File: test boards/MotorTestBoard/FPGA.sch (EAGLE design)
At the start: 2 parts, among them X1 87758-4016, X2 87758-4016

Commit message: FPGA Labelling
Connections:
- new net M11A: X1-3.S
- new net M11B: X1-5.S
- new net M12A: X1-7.S
- new net M12B: X1-9.S
- new net M13A: X1-11.S
- new net M13B: X1-13.S
- new net M1EA: X1-4.S
- new net M1EB: X1-6.S
- new net M1H1: X1-8.S
- new net M1H2: X1-10.S
- new net M1H3: X1-12.S
- new net M21A: X1-27.S
- new net M21B: X1-29.S
- new net M22A: X1-31.S
- new net M22B: X1-33.S
- new net M23A: X1-35.S
- new net M23B: X1-37.S
- new net M2EA: X1-30.S
- new net M2EB: X1-32.S
- new net M2H1: X1-34.S
- new net M2H2: X1-36.S
- new net M2H3: X1-38.S
- new net M31A: X2-4.S
- new net M31B: X2-6.S
- new net M32A: X2-8.S
- new net M32B: X2-10.S
- new net M33A: X2-12.S
- new net M33B: X2-14.S
- new net M3EA: X2-3.S
- new net M3EB: X2-5.S
- new net M3H1: X2-7.S
- new net M3H2: X2-9.S
- new net M3H3: X2-11.S
- new net M41A: X2-28.S
- new net M41B: X2-30.S
- new net M42A: X2-32.S
- new net M42B: X2-34.S
- new net M43A: X2-36.S
- new net M43B: X2-38.S
- new net M4EA: X2-29.S
- new net M4EB: X2-31.S
- new net M4H1: X2-33.S
- new net M4H2: X2-35.S
- new net M4H3: X2-37.S
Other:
- moved on the sheet: X1-1, X1-10, X1-11, X1-12, X1-13, X1-14, X1-15, X1-16, X1-17, X1-18, X1-19, X1-2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

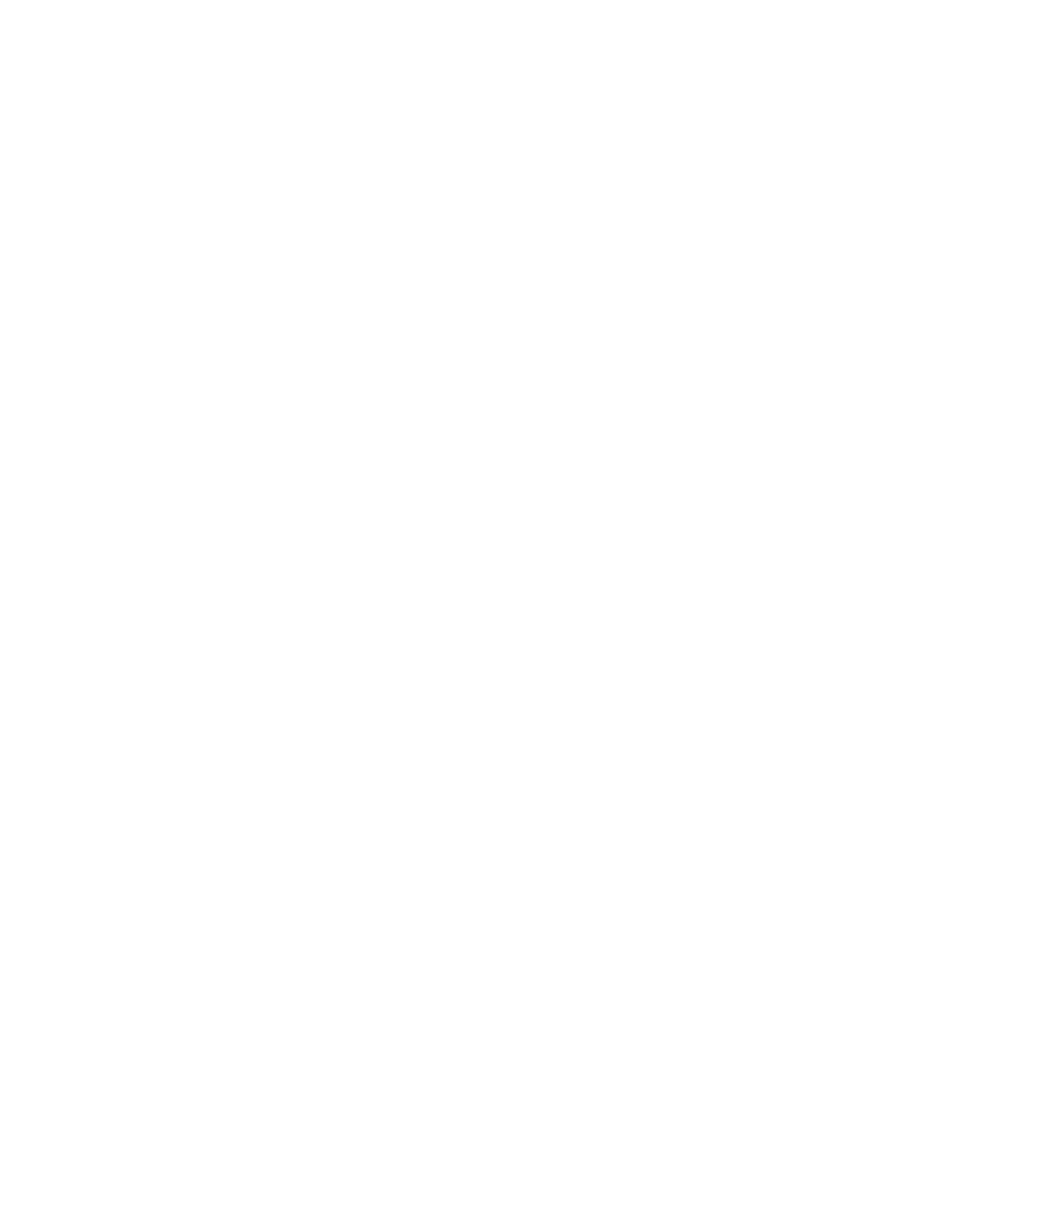
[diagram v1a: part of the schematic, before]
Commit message: motor driver add
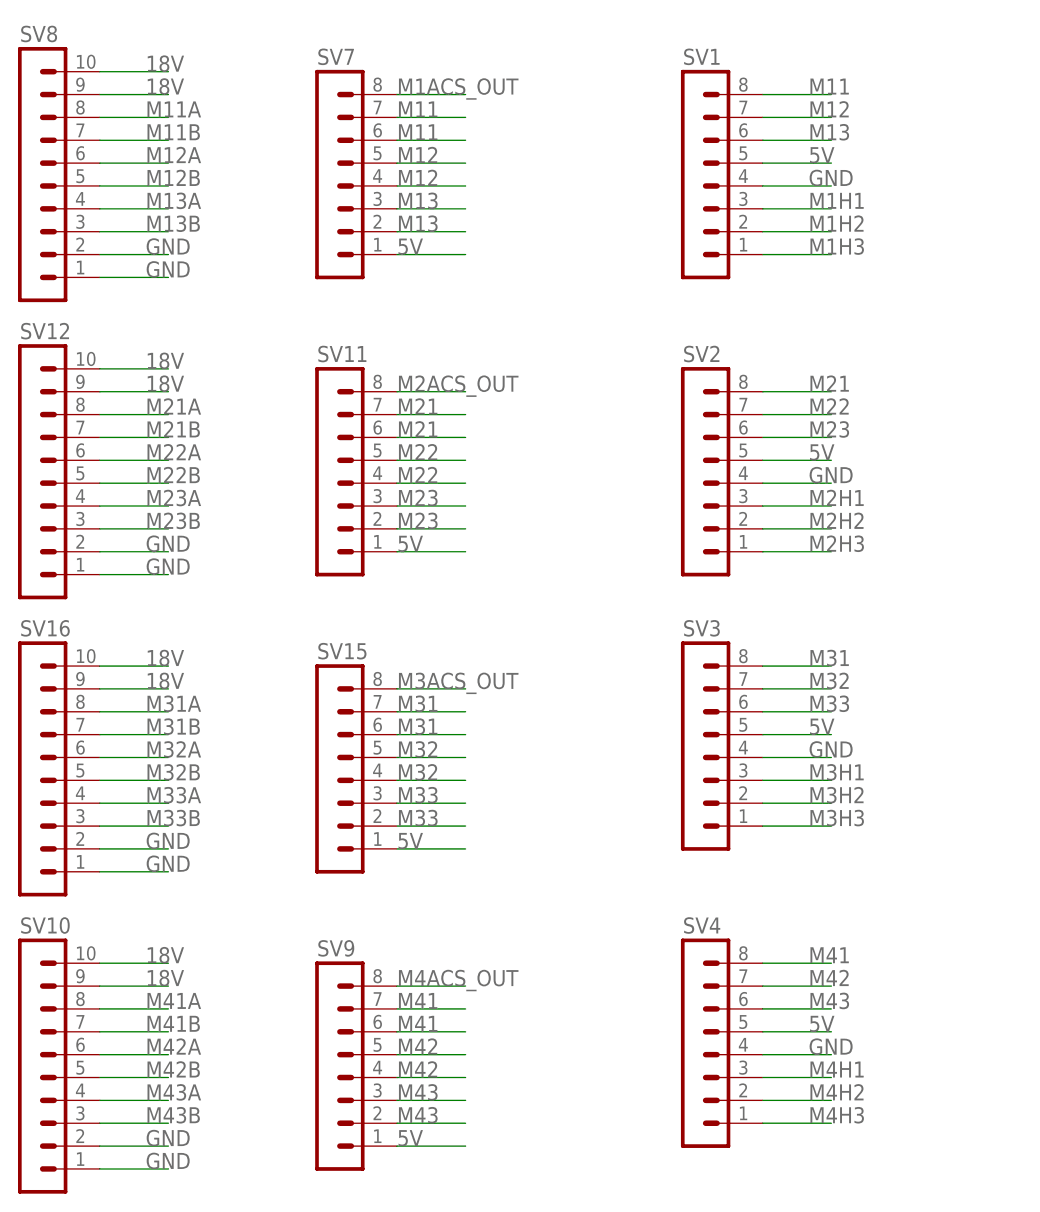
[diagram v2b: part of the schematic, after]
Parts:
- added SV1, SV11, SV15, SV2, SV3, SV4, SV7, SV9: (no value), con-lstb:MA08-1
- added SV10, SV12, SV16, SV8: (no value), con-lstb:MA10-1
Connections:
- new net 18V: SV10.10, SV10.9, SV12.10, SV12.9, SV16.10, SV16.9, SV8.10, SV8.9
- new net 5V: SV1.5, SV11.1, SV15.1, SV2.5, SV3.5, SV4.5, SV7.1, SV9.1
- new net GND: SV1.4, SV10.1, SV10.2, SV12.1, SV12.2, SV16.1, SV16.2, SV2.4, SV3.4, SV4.4, SV8.1, SV8.2
- new net M11: SV1.8, SV7.6, SV7.7
- new net M12: SV1.7, SV7.4, SV7.5
- new net M13: SV1.6, SV7.2, SV7.3
- new net M1ACS_OUT: SV7.8
- new net M21: SV11.6, SV11.7, SV2.8
- new net M22: SV11.4, SV11.5, SV2.7
- new net M23: SV11.2, SV11.3, SV2.6
- new net M2ACS_OUT: SV11.8
- new net M31: SV15.6, SV15.7, SV3.8
- new net M32: SV15.4, SV15.5, SV3.7
- new net M33: SV15.2, SV15.3, SV3.6
- new net M3ACS_OUT: SV15.8
- new net M41: SV4.8, SV9.6, SV9.7
- new net M42: SV4.7, SV9.4, SV9.5
- new net M43: SV4.6, SV9.2, SV9.3
- new net M4ACS_OUT: SV9.8
- net M11A: now also SV8.8
- net M11B: now also SV8.7
- net M12A: now also SV8.6
- net M12B: now also SV8.5
- net M13A: now also SV8.4
- net M13B: now also SV8.3
- net M1H1: now also SV1.3
- net M1H2: now also SV1.2
- net M1H3: now also SV1.1
- net M21A: now also SV12.8
- net M21B: now also SV12.7
- net M22A: now also SV12.6
- net M22B: now also SV12.5
- net M23A: now also SV12.4
- net M23B: now also SV12.3
- net M2H1: now also SV2.3
- net M2H2: now also SV2.2
- net M2H3: now also SV2.1
- net M31A: now also SV16.8
- net M31B: now also SV16.7
- net M32A: now also SV16.6
- net M32B: now also SV16.5
- net M33A: now also SV16.4
- net M33B: now also SV16.3
- net M3H1: now also SV3.3
- net M3H2: now also SV3.2
- net M3H3: now also SV3.1
- net M41A: now also SV10.8
- net M41B: now also SV10.7
- net M42A: now also SV10.6
- net M42B: now also SV10.5
- net M43A: now also SV10.4
- net M43B: now also SV10.3
- net M4H1: now also SV4.3
- net M4H2: now also SV4.2
- net M4H3: now also SV4.1

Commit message: encoders
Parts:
- added J1, J2, J3, J4: (no value), SparkFun-Connectors:CONN_05X2SHD_LOCK
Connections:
- net 5V: now also J1.2, J2.2, J3.2, J4.2
- net GND: now also J1.3, J2.3, J3.3, J4.3
- net M1EA: now also J1.6
- net M1EB: now also J1.8
- net M2EA: now also J2.6
- net M2EB: now also J2.8
- net M3EA: now also J3.6
- net M3EB: now also J3.8
- net M4EA: now also J4.6
- net M4EB: now also J4.8
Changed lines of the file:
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@@
 <layer number="115" name="ReferenceISLANDS" color="7" fill="1" visible="yes" active="yes"/>
 <layer number="116" name="Patch_BOT" color="9" fill="4" visible="yes" active="yes"/>
+<layer number="117" name="BACKMAAT1" color="7" fill="1" visible="yes" active="yes"/>
 <layer number="118" name="Rect_Pads" color="7" fill="1" visible="no" active="no"/>
+<layer number="119" name="KAP_TEKEN" color="7" fill="1" visible="yes" active="yes"/>
+<layer number="120" name="KAP_MAAT1" color="7" fill="1" visible="yes" active="yes"/>
 <layer number="121" name="_tsilk" color="7" fill="1" visible="no" active="yes"/>
 <layer number="122" name="_bsilk" color="7" fill="1" visible="no" active="yes"/>
@@
 <layer number="128" name="_bValues" color="7" fill="1" visible="yes" active="yes"/>
 <layer number="129" name="Mask" color="7" fill="1" visible="yes" active="yes"/>
+<layer number="130" name="SMDSTROOK" color="7" fill="1" visible="yes" active="yes"/>
 <layer number="131" name="tAdjust" color="7" fill="1" visible="yes" active="yes"/>
 <layer number="132" name="bAdjust" color="7" fill="1" visible="yes" active="yes"/>
+<layer number="133" name="bottom_silk" color="7" fill="1" visible="yes" active="yes"/>
+<layer number="134" name="silk_top" color="7" fill="1" visible="yes" active="yes"/>
+<layer number="135" name="silk_bottom" color="7" fill="1" visible="yes" active="yes"/>
+<layer number="136" name="silktop" color="7" fill="1" visible="yes" active="yes"/>
+<layer number="137" name="silkbottom" color="7" fill="1" visible="yes" active="yes"/>
 <layer number="144" name="Drill_legend" color="7" fill="1" visible="no" active="yes"/>
+<layer number="145" name="DrillLegend_01-16" color="7" fill="1" visible="yes" active="yes"/>
+<layer number="146" name="DrillLegend_01-20" color="7" fill="1" visible="yes" active="yes"/>
 <layer number="150" name="Notes" color="7" fill="1" visible="yes" active="yes"/>
 <layer number="151" name="HeatSink" color="7" fill="1" visible="no" active="yes"/>
@@
 <layer number="154" name="FabDoc2" color="7" fill="1" visible="yes" active="yes"/>
 <layer number="155" name="FabDoc3" color="7" fill="1" visible="yes" active="yes"/>
+<layer number="166" name="AntennaArea" color="7" fill="1" visible="yes" active="yes"/>
+<layer number="168" name="4mmHeightArea" color="7" fill="1" visible="yes" active="yes"/>
 <layer number="199" name="Contour" color="7" fill="1" visible="yes" active="yes"/>
 <layer number="200" name="200bmp" color="1" fill="10" visible="no" active="no"/>
@@
 <class number="0" name="default" width="0" drill="0">
 </class>
+<class number="1" name="5v" width="0.4" drill="0.4">
+<clearance class="1" value="0.1524"/>
+</class>
+<class number="3" name="signal" width="0.3" drill="0.4">
+<clearance class="3" value="0.1524"/>
+</class>
+<class number="4" name="gnd" width="1.4" drill="0.4">
+<clearance class="4" value="0.1524"/>
+</class>
 </classes>
 <parts>
@@
 <part name="SV9" library="con-lstb" library_urn="urn:adsk.eagle:library:162" deviceset="MA08-1" device="" package3d_urn="urn:adsk.eagle:package:8343/1"/>
 <part name="SV10" library="con-lstb" library_urn="urn:adsk.eagle:library:162" deviceset="MA10-1" device="" package3d_urn="urn:adsk.eagle:package:8346/1"/>
+<part name="J1" library="SparkFun-Connectors" library_urn="urn:adsk.eagle:library:513" deviceset="CONN_05X2" device="SHD_LOCK" package3d_urn="urn:adsk.eagle:package:38007/1"/>
+<part name="J2" library="SparkFun-Connectors" library_urn="urn:adsk.eagle:library:513" deviceset="CONN_05X2" device="SHD_LOCK" package3d_urn="urn:adsk.eagle:package:38007/1"/>
+<part name="J3" library="SparkFun-Connectors" library_urn="urn:adsk.eagle:library:513" deviceset="CONN_05X2" device="SHD_LOCK" package3d_urn="urn:adsk.eagle:package:38007/1"/>
+<part name="J4" library="SparkFun-Connectors" library_urn="urn:adsk.eagle:library:513" deviceset="CONN_05X2" device="SHD_LOCK" package3d_urn="urn:adsk.eagle:package:38007/1"/>
 </parts>
 <sheets>
@@
 <instance part="SV9" gate="1" x="-45.72" y="-25.4"/>
 <instance part="SV10" gate="1" x="-78.74" y="-25.4"/>
+<instance part="J1" gate="G$1" x="-114.3" y="76.2"/>
+<instance part="J2" gate="G$1" x="-114.3" y="43.18"/>
+<instance part="J3" gate="G$1" x="-116.84" y="12.7"/>
+<instance part="J4" gate="G$1" x="-111.76" y="-17.78"/>
 </instances>
 <busses>
@@
 <label x="68.58" y="60.96" size="1.778" layer="95"/>
 </segment>
+<segment>
+<pinref part="J1" gate="G$1" pin="6"/>
+<wire x1="-106.68" y1="76.2" x2="-104.14" y2="76.2" width="0.1524" layer="91"/>
+<label x="-104.14" y="76.2" size="1.778" layer="95"/>
+</segment>
 </net>
 <net name="M1EB" class="0">
@@
 <wire x1="76.2" y1="58.42" x2="68.58" y2="58.42" width="0.1524" layer="91"/>
 <label x="68.58" y="58.42" size="1.778" layer="95"/>
+</segment>
+<segment>
+<pinref part="J1" gate="G$1" pin="8"/>
+<wire x1="-106.68" y1="73.66" x2="-104.14" y2="73.66" width="0.1524" layer="91"/>
+<label x="-104.14" y="73.66" size="1.778" layer="95"/>
 </segment>
 </net>
@@
 <label x="68.58" y="25.4" size="1.778" layer="95"/>
 </segment>
+<segment>
+<pinref part="J2" gate="G$1" pin="8"/>
+<wire x1="-106.68" y1="40.64" x2="-104.14" y2="40.64" width="0.1524" layer="91"/>
+<label x="-104.14" y="40.64" size="1.778" layer="95"/>
+</segment>
 </net>
 <net name="M2EA" class="0">
@@
 <label x="68.58" y="27.94" size="1.778" layer="95"/>
 </segment>
+<segment>
+<pinref part="J2" gate="G$1" pin="6"/>
+<wire x1="-106.68" y1="43.18" x2="-104.14" y2="43.18" width="0.1524" layer="91"/>
+<label x="-104.14" y="43.18" size="1.778" layer="95"/>
+</segment>
 </net>
 <net name="M3EA" class="0">
@@
 <label x="93.98" y="60.96" size="1.778" layer="95"/>
 </segment>
+<segment>
+<pinref part="J3" gate="G$1" pin="6"/>
+<wire x1="-109.22" y1="12.7" x2="-106.68" y2="12.7" width="0.1524" layer="91"/>
+<label x="-106.68" y="12.7" size="1.778" layer="95"/>
+</segment>
 </net>
 <net name="M3EB" class="0">
@@
 <wire x1="93.98" y1="58.42" x2="99.06" y2="58.42" width="0.1524" layer="91"/>
 <label x="93.98" y="58.42" size="1.778" layer="95"/>
+</segment>
+<segment>
+<pinref part="J3" gate="G$1" pin="8"/>
+<wire x1="-109.22" y1="10.16" x2="-106.68" y2="10.16" width="0.1524" layer="91"/>
+<label x="-106.68" y="10.16" size="1.778" layer="95"/>
 </segment>
 </net>
@@
 <label x="93.98" y="25.4" size="1.778" layer="95"/>
 </segment>
+<segment>
+<pinref part="J4" gate="G$1" pin="8"/>
+<wire x1="-104.14" y1="-20.32" x2="-101.6" y2="-20.32" width="0.1524" layer="91"/>
+<label x="-101.6" y="-20.32" size="1.778" layer="95"/>
+</segment>
 </net>
 <net name="M4EA" class="0">
@@
 <label x="93.98" y="27.94" size="1.778" layer="95"/>
 </segment>
+<segment>
+<pinref part="J4" gate="G$1" pin="6"/>
+<wire x1="-104.14" y1="-17.78" x2="-101.6" y2="-17.78" width="0.1524" layer="91"/>
+<label x="-101.6" y="-17.78" size="1.778" layer="95"/>
+</segment>
 </net>
 <net name="M11" class="0">
@@
 <label x="-38.1" y="-33.02" size="1.778" layer="95"/>
 </segment>
+<segment>
+<pinref part="J1" gate="G$1" pin="2"/>
+<wire x1="-106.68" y1="81.28" x2="-104.14" y2="81.28" width="0.1524" layer="91"/>
+<label x="-104.14" y="81.28" size="1.778" layer="95"/>
+</segment>
+<segment>
+<pinref part="J2" gate="G$1" pin="2"/>
+<wire x1="-106.68" y1="48.26" x2="-104.14" y2="48.26" width="0.1524" layer="91"/>
+<label x="-104.14" y="48.26" size="1.778" layer="95"/>
+</segment>
+<segment>
+<pinref part="J3" gate="G$1" pin="2"/>
+<wire x1="-109.22" y1="17.78" x2="-106.68" y2="17.78" width="0.1524" layer="91"/>
+<label x="-106.68" y="17.78" size="1.778" layer="95"/>
+</segment>
+<segment>
+<pinref part="J4" gate="G$1" pin="2"/>
+<wire x1="-104.14" y1="-12.7" x2="-101.6" y2="-12.7" width="0.1524" layer="91"/>
+<label x="-101.6" y="-12.7" size="1.778" layer="95"/>
+</segment>
 </net>
 <net name="GND" class="0">
@@
 <label x="-66.04" y="-35.56" size="1.778" layer="95"/>
 </segment>
-</net>
+<segment>
+<pinref part="J1" gate="G$1" pin="3"/>
+<wire x1="-121.92" y1="78.74" x2="-124.46" y2="78.74" width="0.1524" layer="91"/>
+<label x="-129.54" y="78.74" size="1.778" layer="95"/>
+</segment>
+<segment>
+<pinref part="J2" gate="G$1" pin="3"/>
+<wire x1="-121.92" y1="45.72" x2="-124.46" y2="45.72" width="0.1524" layer="91"/>
+<label x="-129.54" y="45.72" size="1.778" layer="95"/>
+</segment>
+<segment>
+<pinref part="J3" gate="G$1" pin="3"/>
+<wire x1="-124.46" y1="15.24" x2="-127" y2="15.24" width="0.1524" layer="91"/>
+<label x="-132.08" y="15.24" size="1.778" layer="95"/>
+</segment>
+<segment>
+<pinref part="J4" gate="G$1" pin="3"/>
+<wire x1="-119.38" y1="-15.24" x2="-121.92" y2="-15.24" width="0.1524" layer="91"/>
+<label x="-127" y="-15.24" size="1.778" layer="95"/>
+</segment>
+</net>
